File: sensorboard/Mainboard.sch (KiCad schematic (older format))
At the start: 61 parts, among them J10 Conn_01x02_Male, J2 8P8C_LED, J9 Conn_01x02_Male, Q1 MMDT2222A, U1 CP2102N-A01-GQFN24, U2 SN65HVD230, U3 ESP32-WROOM-32D, U4 W25Q64FV

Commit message: Voltage divider setup
Voltage divider setup, removed unused components, CAN RX/TX empty for now (waiting for kiran)
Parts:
- removed D7: CABLE_DETECT, LED_SMD:LED_0603_1608Metric_Castellated, symbol Device:LED
- removed J2: 8P8C_LED, Connector_RJ:RJ45_Amphenol_RJHSE538X, symbol Connector:8P8C_LED
- removed JP1, JP5: SolderJumper_2_Open, Jumper:SolderJumper-2_P1.3mm_Open_TrianglePad1.0x1.5mm, symbol Jumper:SolderJumper_2_Open
- removed R15, R18, R19: 470, Resistor_SMD:R_0603_1608Metric, symbol Device:R_Small
- removed R20, R23, R31: 10K, Resistor_SMD:R_0603_1608Metric, symbol Device:R_Small
- removed TP1, TP24: TestPoint, TestPoint:TestPoint_THTPad_1.0x1.0mm_Drill0.5mm, symbol Connector:TestPoint
- removed U4: W25Q64FV, Package_SO:SOIC-8_3.9x4.9mm_P1.27mm, symbol Mainboard-rescue:W25Q64FV-iclr
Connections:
- no-connect marks 34 -> 30

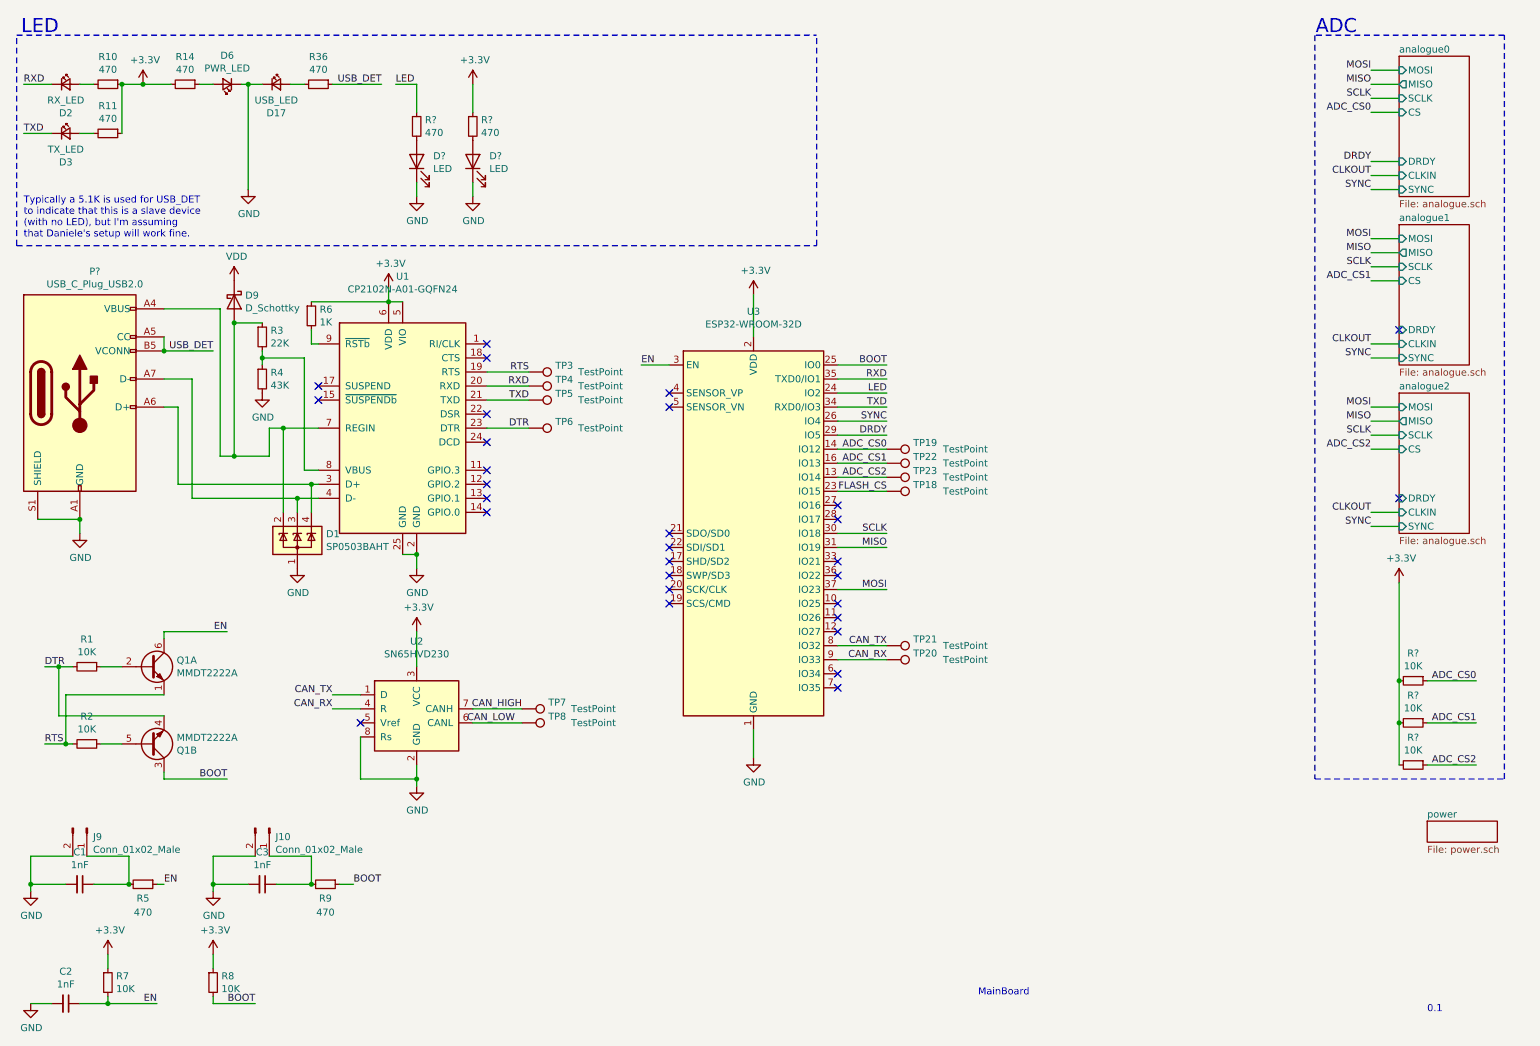
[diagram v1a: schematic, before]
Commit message: I2C ADC conversion+MCP31856 x10
As above xD
just need to do the pcb layout
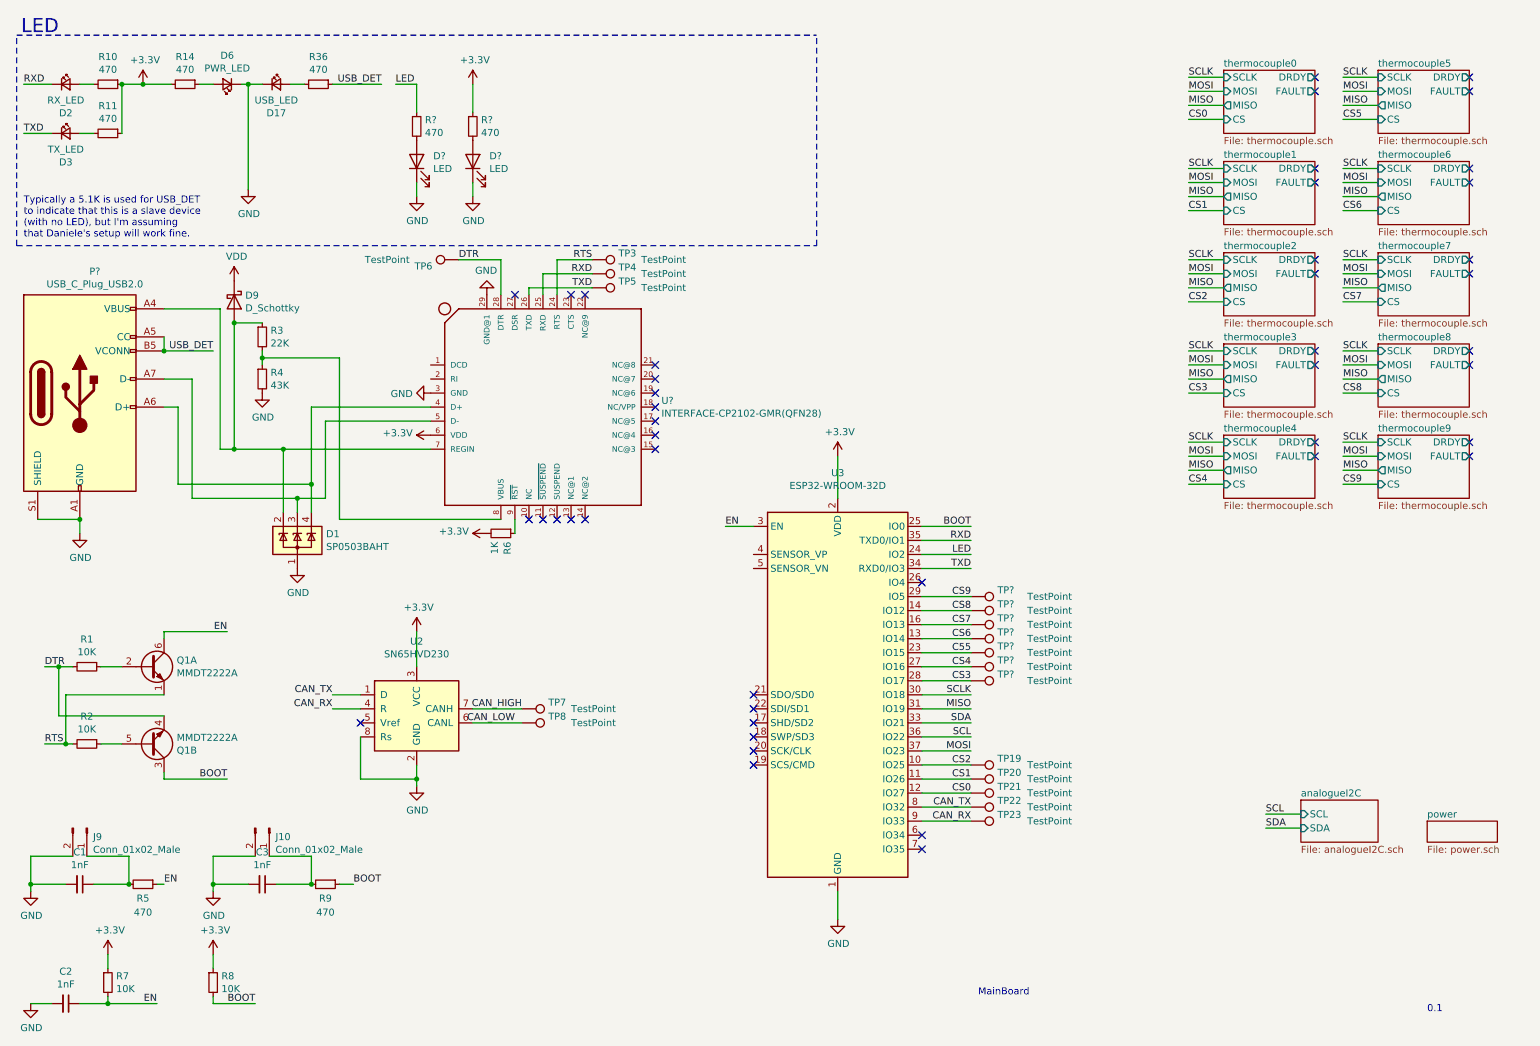
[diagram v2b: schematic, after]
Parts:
- removed R? (x3): 10K, Resistor_SMD:R_0603_1608Metric, symbol Device:R_Small
- removed TP18: TestPoint, TestPoint:TestPoint_THTPad_1.0x1.0mm_Drill0.5mm, symbol Connector:TestPoint
- removed U1: CP2102N-A01-GQFN24, Package_DFN_QFN:QFN-24-1EP_4x4mm_P0.5mm_EP2.6x2.6mm_ThermalVias, symbol Interface_USB:CP2102N-A01-GQFN24
- added TP? (x7): TestPoint, TestPoint:TestPoint_THTPad_1.0x1.0mm_Drill0.5mm, symbol Connector:TestPoint
- added U?: INTERFACE-CP2102-GMR(QFN28), QFN28G_0.5-5X5MM, symbol iclr:INTERFACE-CP2102-GMR(QFN28)
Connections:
- net +3V3: now also R6.2, U?.6 (VDD); no longer R6.1
- net CAN_RX: now also TP23.1; no longer TP20.1
- net CAN_TX: now also TP22.1; no longer TP21.1
- net DTR: now also U?.28 (DTR)
- net GND: now also U?.29 (GND@1), U?.3 (GND)
- net RTS: now also U?.24 (RTS)
- net RXD: now also U?.25 (RXD)
- net TXD: now also U?.26 (TXD)
- net CS2: now reaches U3.10 (IO25)
- net CS2: now also TP19.1
- net CS1: now reaches U3.11 (IO26)
- net CS1: now also TP20.1
- net CS0: now reaches U3.12 (IO27)
- net CS0: now also TP21.1
- net CS4: now reaches U3.27 (IO16)
- net CS4: now also TP?.1
- net CS3: now reaches U3.28 (IO17)
- net CS3: now also TP?.1
- net SDA: now reaches U3.33 (IO21)
- net SCL: now reaches U3.36 (IO22)
- net at D1.4 (K), P?.A6 (D+): now also U?.4 (D+)
- net at D1.3 (K), P?.A7 (D-): now also U?.5 (D-)
- net at D1.2 (K), D9.2 (A), P?.A4 (VBUS)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: now also U?.7 (REGIN)
- net at R3.2, R4.1: now also U?.8 (VBUS)
- net ADC_CS0 renamed CS8
- net CS8: now also TP?.1; no longer TP19.1
- net ADC_CS1 renamed CS7
- net CS7: now also TP?.1; no longer TP22.1
- net ADC_CS2 renamed CS6
- net CS6: now also TP?.1; no longer TP23.1
- net DRDY renamed CS9
- net CS9: now also TP?.1
- net FLASH_CS renamed C55
- net C55: now also TP?.1
- net SYNC: no longer names the net of U3.26 (IO4)
- new net: R6.1, U?.9 (~RST)
- no-connect marks 30 -> 45
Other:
- note removed: "ADC"
- moved on the sheet: R6, TP19, TP20, TP21, TP22, TP23, TP3, TP4, TP5, TP6, U3

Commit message: Antenna
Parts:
- added ANT? (x2): AMCA31-2R450G-S1F-T3, ANT_AMCA31-2R450G-S1F-T3, symbol AMCA31-2R450G-S1F-T3:AMCA31-2R450G-S1F-T3
- added C?: 1.2pF, symbol Device:C_Small
- added C?: 1.5pF, symbol Device:C_Small
- added L?: 1.8nH, symbol Device:L_Small
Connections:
- net GND: now also C?.1, C?.1
- net LNA_IN: now reaches U3.26 (IO4)
- net LNA_IN: now also C?.2, L?.2
- new net: ANT?.1, C?.2, L?.1
- no-connect marks 45 -> 44
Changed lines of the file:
@@
 Wire Wire Line
 	7350 4650 7000 4650
-NoConn ~ 7000 4550
 Text Label 8900 950  0    50   ~ 0
 SCLK
@@
 NoConn ~ 7000 6350
 NoConn ~ 7000 6450
+$Comp
+L AMCA31-2R450G-S1F-T3:AMCA31-2R450G-S1F-T3 ANT?
+U 1 1 619C5032
+P 8300 3050
+F 0 "ANT?" H 8050 3200 50  0000 L CNN
+F 1 "AMCA31-2R450G-S1F-T3" H 7250 3100 50  0000 L CNN
+F 2 "ANT_AMCA31-2R450G-S1F-T3" H 8300 3050 50  0001 L BNN
+F 3 "" H 8300 3050 50  0001 L BNN
+F 4 "1.4mm" H 8300 3050 50  0001 L BNN "MAXIMUM_PACKAGE_HEIGHT"
+F 5 "05.17.2017" H 8300 3050 50  0001 L BNN "PARTREV"
+F 6 "Manufacturer Recommendation" H 8300 3050 50  0001 L BNN "STANDARD"
+F 7 "ABRACON" H 8300 3050 50  0001 L BNN "MANUFACTURER"
+	1    8300 3050
+	1    0    0    -1
+$EndComp
+$Comp
+L AMCA31-2R450G-S1F-T3:AMCA31-2R450G-S1F-T3 ANT?
+U 1 1 619C510D
+P 4000 6850
+F 0 "ANT?" H 4125 6947 50  0000 L CNN
+F 1 "AMCA31-2R450G-S1F-T3" H 4125 6856 50  0000 L CNN
+F 2 "ANT_AMCA31-2R450G-S1F-T3" H 4000 6850 50  0001 L BNN
+F 3 "" H 4000 6850 50  0001 L BNN
+F 4 "1.4mm" H 4000 6850 50  0001 L BNN "MAXIMUM_PACKAGE_HEIGHT"
+F 5 "05.17.2017" H 4000 6850 50  0001 L BNN "PARTREV"
+F 6 "Manufacturer Recommendation" H 4000 6850 50  0001 L BNN "STANDARD"
+F 7 "ABRACON" H 4000 6850 50  0001 L BNN "MANUFACTURER"
+	1    4000 6850
+	1    0    0    -1
+$EndComp
+$Comp
+L Device:C_Small C?
+U 1 1 619DACB2
+P 8500 3400
+F 0 "C?" V 8271 3400 50  0000 C CNN
+F 1 "1.2pF" V 8362 3400 50  0000 C CNN
+F 2 "" H 8500 3400 50  0001 C CNN
+F 3 "~" H 8500 3400 50  0001 C CNN
+	1    8500 3400
+	0    1    1    0
+$EndComp
+$Comp
+L Device:C_Small C?
+U 1 1 619DB8D6
+P 8500 3800
+F 0 "C?" V 8700 3800 50  0000 C CNN
+F 1 "1.5pF" V 8600 3800 50  0000 C CNN
+F 2 "" H 8500 3800 50  0001 C CNN
+F 3 "~" H 8500 3800 50  0001 C CNN
+	1    8500 3800
+	0    1    1    0
+$EndComp
+$Comp
+L Device:L_Small L?
+U 1 1 619DC309
+P 8300 3600
+F 0 "L?" H 8348 3646 50  0000 L CNN
+F 1 "1.8nH" H 8348 3555 50  0000 L CNN
+F 2 "" H 8300 3600 50  0001 C CNN
+F 3 "~" H 8300 3600 50  0001 C CNN
+	1    8300 3600
+	1    0    0    -1
+$EndComp
+$Comp
+L power:GND #PWR?
+U 1 1 619DCD9E
+P 8600 3400
+F 0 "#PWR?" H 8600 3150 50  0001 C CNN
+F 1 "GND" V 8605 3272 50  0000 R CNN
+F 2 "" H 8600 3400 50  0001 C CNN
+F 3 "" H 8600 3400 50  0001 C CNN
+	1    8600 3400
+	0    -1   -1   0
+$EndComp
+$Comp
+L power:GND #PWR?
+U 1 1 619DD718
+P 8600 3800
+F 0 "#PWR?" H 8600 3550 50  0001 C CNN
+F 1 "GND" V 8605 3672 50  0000 R CNN
+F 2 "" H 8600 3800 50  0001 C CNN
+F 3 "" H 8600 3800 50  0001 C CNN
+	1    8600 3800
+	0    -1   -1   0
+$EndComp
+Wire Wire Line
+	8300 3250 8300 3400
+Wire Wire Line
+	8400 3400 8300 3400
+Connection ~ 8300 3400
+Wire Wire Line
+	8300 3400 8300 3500
+Wire Wire Line
+	8300 3700 8300 3800
+Wire Wire Line
+	8300 3800 8400 3800
+Text Label 7350 4550 2    50   ~ 0
+LNA_IN
+Wire Wire Line
+	7350 4550 7000 4550
+Text Label 8300 4100 1    50   ~ 0
+LNA_IN
+Wire Wire Line
+	8300 4100 8300 3800
+Connection ~ 8300 3800
 $EndSCHEMATC

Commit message: Small edits
removed a floating extra antenna
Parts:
- removed ANT?: AMCA31-2R450G-S1F-T3, ANT_AMCA31-2R450G-S1F-T3, symbol AMCA31-2R450G-S1F-T3:AMCA31-2R450G-S1F-T3
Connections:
- net +3V3: now also U2.4 (R); no longer U2.3 (VCC)
- net CAN_HIGH: no longer U2.7 (CANH)
- net CAN_LOW: no longer U2.6 (CANL)
- net CAN_RX: now also U2.2 (GND); no longer U2.4 (R)
- net CAN_TX: no longer U2.1 (D)
- net GND: now also U2.7 (CANH); no longer U2.2 (GND), U2.8 (Rs)
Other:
- moved on the sheet: U2
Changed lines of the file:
@@
 Connection ~ 1300 1000
 Wire Wire Line
-	3400 4900 3400 5150
+	3400 4900 3400 5050
 $Comp
 L Interface_CAN_LIN:SN65HVD230 U2
@@
 F 3 "http://www.ti.com/lit/ds/symlink/sn65hvd230.pdf" H 3300 5850 50  0001 C CNN
 	1    3400 5450
-	1    0    0    -1
+	0    1    1    0
 $EndComp
 NoConn ~ 3000 5550
@@
 $EndComp
 $Comp
-L AMCA31-2R450G-S1F-T3:AMCA31-2R450G-S1F-T3 ANT?
-U 1 1 619C510D
-P 4000 6850
-F 0 "ANT?" H 4125 6947 50  0000 L CNN
-F 1 "AMCA31-2R450G-S1F-T3" H 4125 6856 50  0000 L CNN
-F 2 "ANT_AMCA31-2R450G-S1F-T3" H 4000 6850 50  0001 L BNN
-F 3 "" H 4000 6850 50  0001 L BNN
-F 4 "1.4mm" H 4000 6850 50  0001 L BNN "MAXIMUM_PACKAGE_HEIGHT"
-F 5 "05.17.2017" H 4000 6850 50  0001 L BNN "PARTREV"
-F 6 "Manufacturer Recommendation" H 4000 6850 50  0001 L BNN "STANDARD"
-F 7 "ABRACON" H 4000 6850 50  0001 L BNN "MANUFACTURER"
-	1    4000 6850
-	1    0    0    -1
-$EndComp
-$Comp
 L Device:C_Small C?
 U 1 1 619DACB2
@@
 	8300 4100 8300 3800
 Connection ~ 8300 3800
+Connection ~ 3400 5050
+Wire Wire Line
+	3400 5050 3400 5150
 $EndSCHEMATC
